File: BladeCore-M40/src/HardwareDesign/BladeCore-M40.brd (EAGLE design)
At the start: 22 x 42 mm, 76 parts, among them IC1 CAT24C512HU5IGT3, IC2 PI3USB102J, IC3 W25Q128JVPIQ, IC4 RP2040, IC5 MCP6001R, IC6 MIC5504-3.3YM5-TR, IC7 FT232RNQ, IC8 AP7335-WG-7, X1 12MHz

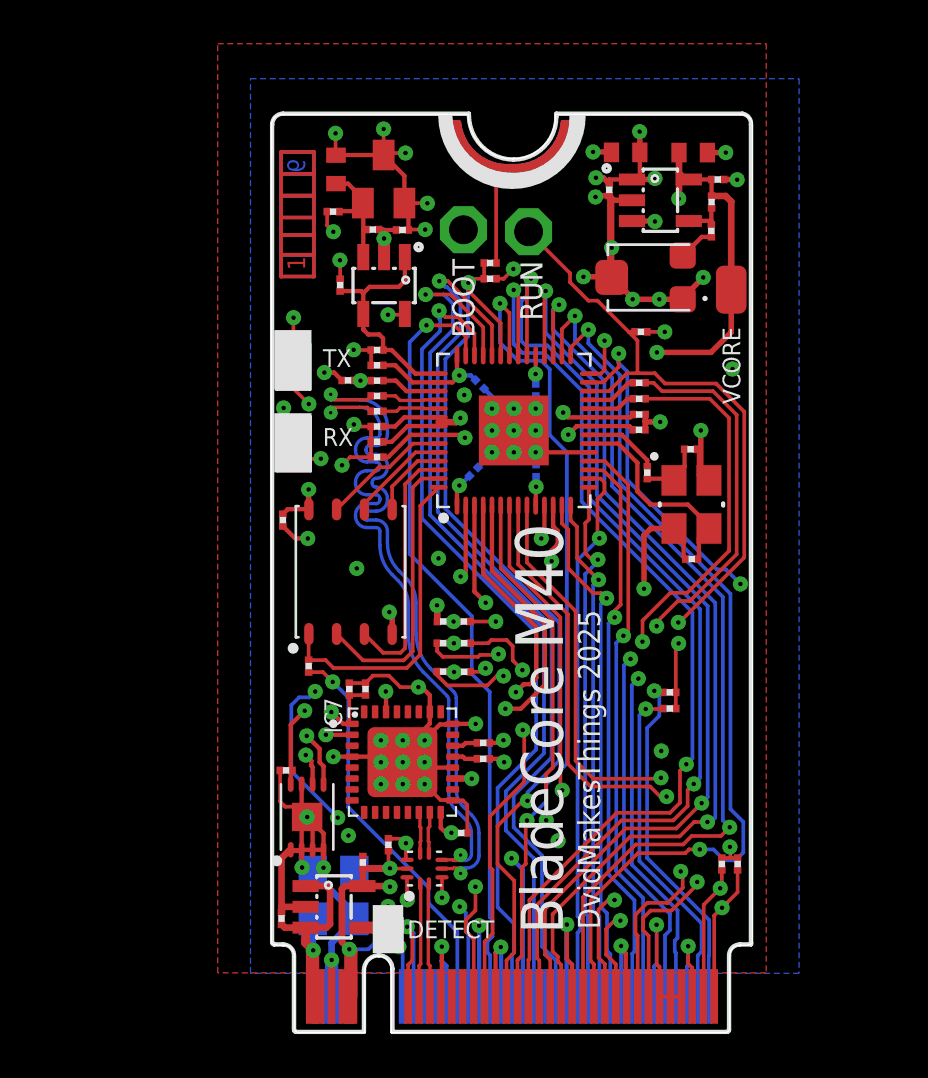
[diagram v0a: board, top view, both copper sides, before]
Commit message: Finish M40 design
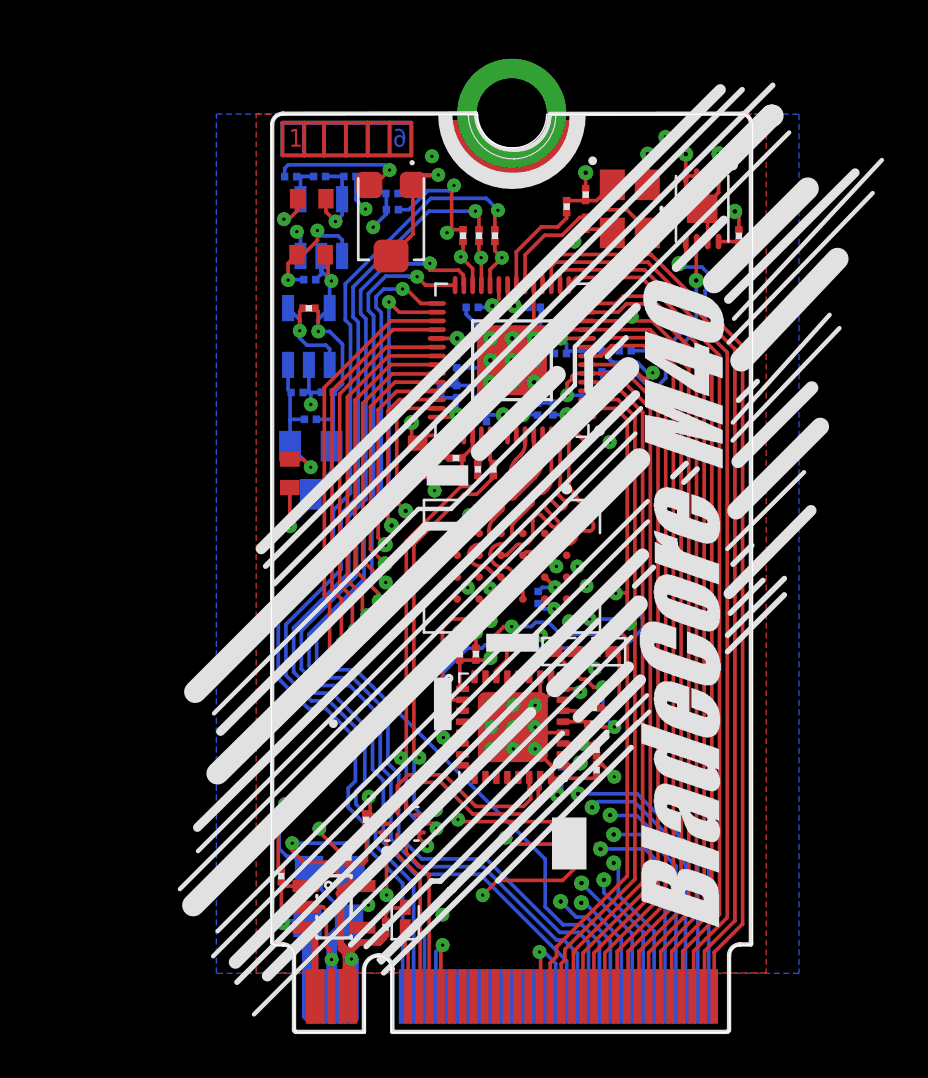
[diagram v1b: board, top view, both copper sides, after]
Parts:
- removed BOOT, RUN: TPPAD1-13, testpad:P1-13
- removed R25, R26: 10K, ds_passive:R0201
- removed VCORE: TP, ds_passive:TP
- added R17, R3, R4: 0R, ds_passive:R0201
- added R18: DNI, ds_passive:R0201
- added U$1: (no value), ds_silkscreen:DMT
- C21: value 100nF -> 4.7uF; device ds_passive:0201 -> ds_passive:C0402
- IC3: value W25Q128JVPIQ -> W25Q128JVCIQ TR; device MCU:SON127P600X500X75-8N -> ds_ic_memory:BGA24C100P4X6_800X600X120N
- IC4: value RP2040 -> RP-2040; device ds_ic_mcu:QFN40P700X700X100-57T510 -> ds_ic_mcu:QFN56
- IC7: device ftdichip:QFN32 -> ds_ic_peripherals:QFN32
- R11: value 1K -> 0R
- R23, R24: value 10K -> 3.3K
- R30: value 0R -> DNI
- RX: value CHIP-FLAT-G_0603-0.35MM -> CHIP-FLAT-G_0402; device LED:LEDC1608X35N_FLAT-G -> LED:LEDC1005X25N_FLAT-G
- TX: value CHIP-FLAT-B_0603-0.35MM -> CHIP-FLAT-B_0402; device LED:LEDC1608X35N_FLAT-B -> LED:LEDC1005X25N_FLAT-B
- moved IC1 33.2 mm to (22.2, 40.0), turned to 270 degrees
- moved C7 32.0 mm to (23.9, 38.7), turned to 90 degrees
- moved R5 27.5 mm to (16.1, 10.2), turned to 0 degrees
- moved R7 26.1 mm to (16.1, 10.9), turned to 180 degrees
- moved R24 24.3 mm to (17.3, 33.4), flipped to the bottom, turned to 180 degrees
- moved R23 23.2 mm to (17.3, 32.5), flipped to the bottom, turned to 180 degrees
- moved R28 19.4 mm to (3.35, 41.4), flipped to the bottom, turned to 0 degrees
- moved TX 18.2 mm to (15.9, 19.7), turned to 0 degrees
- moved R27 18.0 mm to (4.67, 41.4), flipped to the bottom, turned to 0 degrees
- moved C31 17.6 mm to (4.31, 40.4), turned to 180 degrees
- moved RX 17.1 mm to (17.6, 19.7), turned to 180 degrees
- moved C9 16.8 mm to (6.06, 41.4), flipped to the bottom, turned to 180 degrees
- moved C28 16.1 mm to (16.8, 39.3), turned to 270 degrees
- moved IC8 15.6 mm to (4.75, 39.1), flipped to the bottom, turned to 0 degrees
- moved C30 15.1 mm to (4.28, 37.9), turned to 0 degrees
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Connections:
- net N$1 renamed VFB
- net N$3 renamed FBTRIM
- net N$4 renamed FT_TX
- net N$5 renamed FT_RX
- removed net GP25/USBSEL: IC2.10, IC4.37, M.2-M1.P$39, R5.2, R7.1
- removed net I2C1_SCL: IC1.6, IC4.5, M.2-M1.P$4, R25.2
- removed net I2C1_SDA: IC1.5, IC4.4, M.2-M1.P$2, R26.2
- removed net N$7: IC4.45, R30.1
- removed net SPI0_CS: IC4.28, M.2-M1.P$21
- removed net SPI0_MISO: IC4.27, M.2-M1.P$19
- removed net SPI0_MOSI: IC4.30, M.2-M1.P$25
- removed net SPI0_SCK: IC4.29, M.2-M1.P$23
- removed net SPI1_CS: IC4.16, M.2-M1.P$26
- removed net SPI1_MISO: IC4.15, M.2-M1.P$24
- removed net SPI1_MOSI: IC4.14, M.2-M1.P$22
- removed net SPI1_SCLK: IC4.13, M.2-M1.P$20
- removed net UART0_RX: IC4.3, R31.1
- removed net UART0_TX: IC4.2, R29.2
- removed net UART1_RX: IC4.12, M.2-M1.P$8, R12.2
- removed net UART1_TX: IC4.11, M.2-M1.P$10, R13.1
- removed net USB_BOOT: BOOT.TP, M.2-M1.P$48, R11.1
- new net DETECT: DETECT.C, M.2-M1.P$57
- new net GP0: IC4.2, M.2-M1.P$31, R29.2
- new net GP1: IC4.3, M.2-M1.P$29, R31.1
- new net GP10: IC4.13, M.2-M1.P$11
- new net GP11: IC4.14, M.2-M1.P$9
- new net GP12: IC4.15, M.2-M1.P$7
- new net GP13: IC4.16, M.2-M1.P$5
- new net GP16: IC4.27, M.2-M1.P$28
- new net GP17: IC4.28, M.2-M1.P$26
- new net GP18: IC4.29, M.2-M1.P$24
- new net GP19: IC4.30, M.2-M1.P$22
- new net GP2: IC4.4, M.2-M1.P$27
- new net GP25: IC4.37, M.2-M1.P$10, R11.2
- new net GP3: IC4.5, M.2-M1.P$25
- new net GP4: IC4.6, M.2-M1.P$23, R23.2, R4.1
- new net GP5: IC4.7, M.2-M1.P$21, R24.2, R3.1
- new net GP8: IC4.11, M.2-M1.P$15, R13.1
- new net GP9: IC4.12, M.2-M1.P$13, R12.2
- new net MUXSEL: IC2.10, R11.1, R5.2, R7.1
- new net VREGO: C23.1, IC4.45, R30.1
- net !QSPI_SS: now also IC3.C2; no longer IC3.1, R11.2
- net +3V3_MCU: now also IC3.B4, R17.1; no longer IC3.8, IC8.3, R25.1, R26.1
- net AD0: now also M.2-M1.P$8; no longer M.2-M1.P$30
- net AD1: now also M.2-M1.P$6; no longer M.2-M1.P$34
- net AD2: now also M.2-M1.P$4; no longer M.2-M1.P$38
- net AD3: now also M.2-M1.P$2; no longer M.2-M1.P$42
- net GND: now also IC3.B3, IC4.PAD, M.2-M1.P$30, M.2-M1.P$33, M.2-M1.P$52, R18.2; no longer IC3.4, IC4.57, M.2-M1.P$11, M.2-M1.P$12, M.2-M1.P$17, M.2-M1.P$18, M.2-M1.P$27, M.2-M1.P$28, M.2-M1.P$36, M.2-M1.P$40, M.2-M1.P$41, M.2-M1.P$44, M.2-M1.P$5, M.2-M1.P$50, M.2-M1.P$56, M.2-M1.P$57, M.2-M1.P$6, M.2-M1.P$7, M.2-M1.P$9
- net GP14: now also M.2-M1.P$3; no longer M.2-M1.P$16
- net GP15: now also M.2-M1.P$1; no longer M.2-M1.P$14
- net GP20: now also M.2-M1.P$20; no longer M.2-M1.P$29
- net GP21: now also M.2-M1.P$18; no longer M.2-M1.P$31
- net GP22: now also M.2-M1.P$16; no longer M.2-M1.P$33
- net GP23: now also M.2-M1.P$14; no longer M.2-M1.P$35
- net GP24: now also M.2-M1.P$12; no longer M.2-M1.P$37
- net GP6: now also M.2-M1.P$19; no longer M.2-M1.P$13
- net GP7: now also M.2-M1.P$17; no longer M.2-M1.P$15
- net I2C0_SCL: now also IC1.6, R3.2; no longer IC4.7, M.2-M1.P$3, R23.2
- net I2C0_SDA: now also IC1.5, R4.2; no longer IC4.6, M.2-M1.P$1, R24.2
- net N$2: now also IC8.3, R17.2, R18.1; no longer DETECT.C, M.2-M1.P$58
- net QSPI_SCLK: now also IC3.B2; no longer IC3.6
- net QSPI_SD0: now also IC3.D3; no longer IC3.5
- net QSPI_SD1: now also IC3.D2; no longer IC3.2
- net QSPI_SD2: now also IC3.C4; no longer IC3.3
- net QSPI_SD3: now also IC3.D4; no longer IC3.7
- net RUN: now also M.2-M1.P$54; no longer M.2-M1.P$46, RUN.TP
- net SWCLK_M2: now also M.2-M1.P$58; no longer M.2-M1.P$43
- net SWDIO_M2: now also M.2-M1.P$56; no longer M.2-M1.P$45
- net VCORE: no longer C23.1, VCORE.TP
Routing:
- net GP8: track 0.00 -> 71.2 mm, vias 0 -> 3
- net GP9: track 0.00 -> 58.0 mm, vias 0 -> 2
- net GP25/USBSEL: track 54.0 -> 0.00 mm, vias 3 -> 0
- net GP25: track 0.00 -> 51.5 mm, vias 0 -> 3
- net I2C1_SDA: track 48.2 -> 0.00 mm, vias 3 -> 0
- net GP16: track 0.00 -> 47.2 mm, vias 0 -> 1
- net I2C1_SCL: track 46.8 -> 0.00 mm, vias 3 -> 0
- net USB_BOOT: track 46.4 -> 0.00 mm, vias 1 -> 0
- net GP17: track 0.00 -> 46.1 mm, vias 0 -> 1
- net GP18: track 0.00 -> 45.1 mm, vias 0 -> 1
- net GP0: track 0.00 -> 43.7 mm, vias 0 -> 2
- net SPI0_CS: track 43.1 -> 0.00 mm, vias 2 -> 0
- net GND: track 163.9 -> 121.6 mm, vias 68 -> 53
- net GP19: track 0.00 -> 42.2 mm, vias 0 -> 1
- net SPI0_SCK: track 41.1 -> 0.00 mm, vias 2 -> 0
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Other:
- outline, holes or cut-outs redrawn
- board text removed: "BladeCore"
- board text removed: "M40"

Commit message: update readme
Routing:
- net GP9: track 58.0 -> 56.5 mm
- net GP8: track 71.2 -> 70.2 mm
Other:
- board text added: "J1"
- board text added: "J2"
- board text added: "J3"
- board text added: "M1"
- board text added: "M2"
- board text added: "M3"
- board text added: "R11/01"
- board text added: "R3"
- board text added: "R4"
- board text added: "T01"
- board text added: "T11"
- board text added: "VCORE"
